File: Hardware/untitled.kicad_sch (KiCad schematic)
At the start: 15 parts, among them IC1 LM74502HDDFR, J3 CarLVPowerConnector, Q2 PSMN8R5-40MSDX

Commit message: BPS-Leader Schematic completed (mostly)
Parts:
- renumbered R18 to R51
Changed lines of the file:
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@@
 		(dnp no)
 		(fields_autoplaced yes)
-		(property "Reference" "R18"
+		(property "Reference" "R51"
 			(at 123.19 81.28 90)
 			(effects
@@
 			(project "BPS-Leader"
 				(path "/fb37da34-e420-4994-8cc1-079e8c0fa48e/a39d8cf5-dc9c-4f60-80f8-399517c69b53"
-					(reference "R18")
+					(reference "R51")
 					(unit 1)
 				)

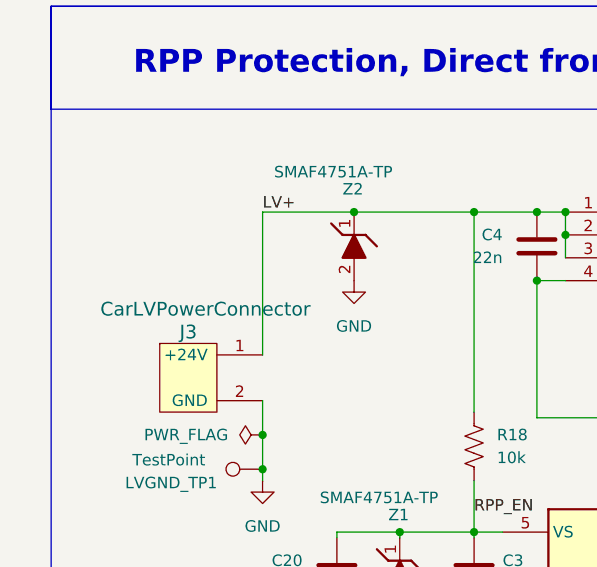
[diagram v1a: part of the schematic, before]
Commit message: added fuse, made kiCad Sharepoint a submodule, added a pulldown, added test-points
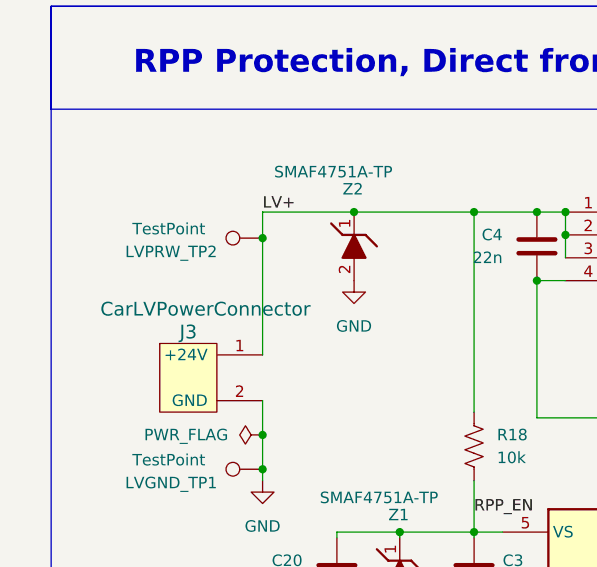
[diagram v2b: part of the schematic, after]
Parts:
- added LVPRW_TP2: TestPoint, UTSVT_Special:TestPoint_HEX_3mmID, symbol Connector:TestPoint
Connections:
- net LV+: now also LVPRW_TP2.1
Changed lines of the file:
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@@
+	)
+	(junction
+		(at 50.165 51.1574)
+		(diameter 0)
+		(color 0 0 0 0)
 	)
 	(junction
@@
 	(wire
 		(pts
+			(xy 50.165 51.1574) (xy 50.165 64.135)
+		)
+		(stroke
+			(width 0)
+			(type default)
+		)
+	)
+	(wire
+		(pts
 			(xy 73.66 48.26) (xy 80.645 48.26)
 		)
@@
 	(wire
 		(pts
-			(xy 50.165 48.26) (xy 50.165 64.135)
+			(xy 50.165 48.26) (xy 50.165 51.1574)
 		)
 		(stroke
@@
 					(unit 1)
 				)
+			)
+		)
+	)
+	(symbol
+		(lib_id "Connector:TestPoint")
+		(at 50.165 51.1574 90)
+		(unit 1)
+		(exclude_from_sim no)
+		(in_bom yes)
+		(on_board yes)
+		(dnp no)
+		(property "Reference" "LVPRW_TP2"
+			(at 40.005 52.6814 90)
+			(effects
+				(font
+					(size 1.27 1.27)
+				)
+			)
+		)
+		(property "Value" "TestPoint"
+			(at 39.751 50.1414 90)
+			(effects
+				(font
+					(size 1.27 1.27)
+				)
+			)
+		)
+		(property "Footprint" "UTSVT_Special:TestPoint_HEX_3mmID"
+			(at 50.165 46.0774 0)
+			(effects
+				(font
+					(size 1.27 1.27)
+				)
+				(hide yes)
+			)
+		)
+		(property "Datasheet" "~"
+			(at 50.165 46.0774 0)
+			(effects
+				(font
+					(size 1.27 1.27)
+				)
+				(hide yes)
+			)
+		)
+		(property "Description" "test point"
+			(at 50.165 51.1574 0)
+			(effects
+				(font
+					(size 1.27 1.27)
+				)
+				(hide yes)
+			)
+		)
+		(pin "1"
+		)
+		(instances
+			(project "BPS-Leader"
+				(path "/fb37da34-e420-4994-8cc1-079e8c0fa48e/a39d8cf5-dc9c-4f60-80f8-399517c69b53"
+					(reference "LVPRW_TP2")
+					(unit 1)
+				)

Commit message: Very, very intial layout designed. Many issues. Too bad!
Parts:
- 24V_TP1, LVGND_TP1, LVPRW_TP2: footprint UTSVT_Special:TestPoint_HEX_3mmID -> TestPoint:TestPoint_Pad_1.0x1.0mm
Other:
- note added: "3.3V injector"
- note removed: "3v3 injector"
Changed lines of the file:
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@@
 		)
 	)
-	(text "3v3 injector"
+	(text "3.3V injector"
 		(exclude_from_sim no)
 		(at 47.244 134.112 0)
@@
 			)
 		)
-		(property "Footprint" "UTSVT_Special:TestPoint_HEX_3mmID"
+		(property "Footprint" "TestPoint:TestPoint_Pad_1.0x1.0mm"
 			(at 50.165 71.755 0)
 			(effects
@@
 			)
 		)
-		(property "Footprint" "UTSVT_Special:TestPoint_HEX_3mmID"
+		(property "Footprint" "TestPoint:TestPoint_Pad_1.0x1.0mm"
 			(at 118.11 52.705 0)
 			(effects
@@
 			)
 		)
-		(property "Footprint" "UTSVT_Special:TestPoint_HEX_3mmID"
+		(property "Footprint" "TestPoint:TestPoint_Pad_1.0x1.0mm"
 			(at 50.165 46.0774 0)
 			(effects

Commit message: Backup
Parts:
- added D12: CDBC560-G, Schlotty:DIOM7959X262N, symbol Schott:CDBC560-G
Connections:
- net LV+: now also D12.2 (A); no longer C4.2, Q2.1 (S_1), Q2.2 (S_2), Q2.3 (S_3), R18.1
- new net: C4.2, D12.1 (K), Q2.1 (S_1), Q2.2 (S_2), Q2.3 (S_3), R18.1
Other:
- moved on the sheet: 24V_TP1, C20, C21, C3, C4, IC1, J3, LVGND_TP1, LVPRW_TP2, Q2, R18, R28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

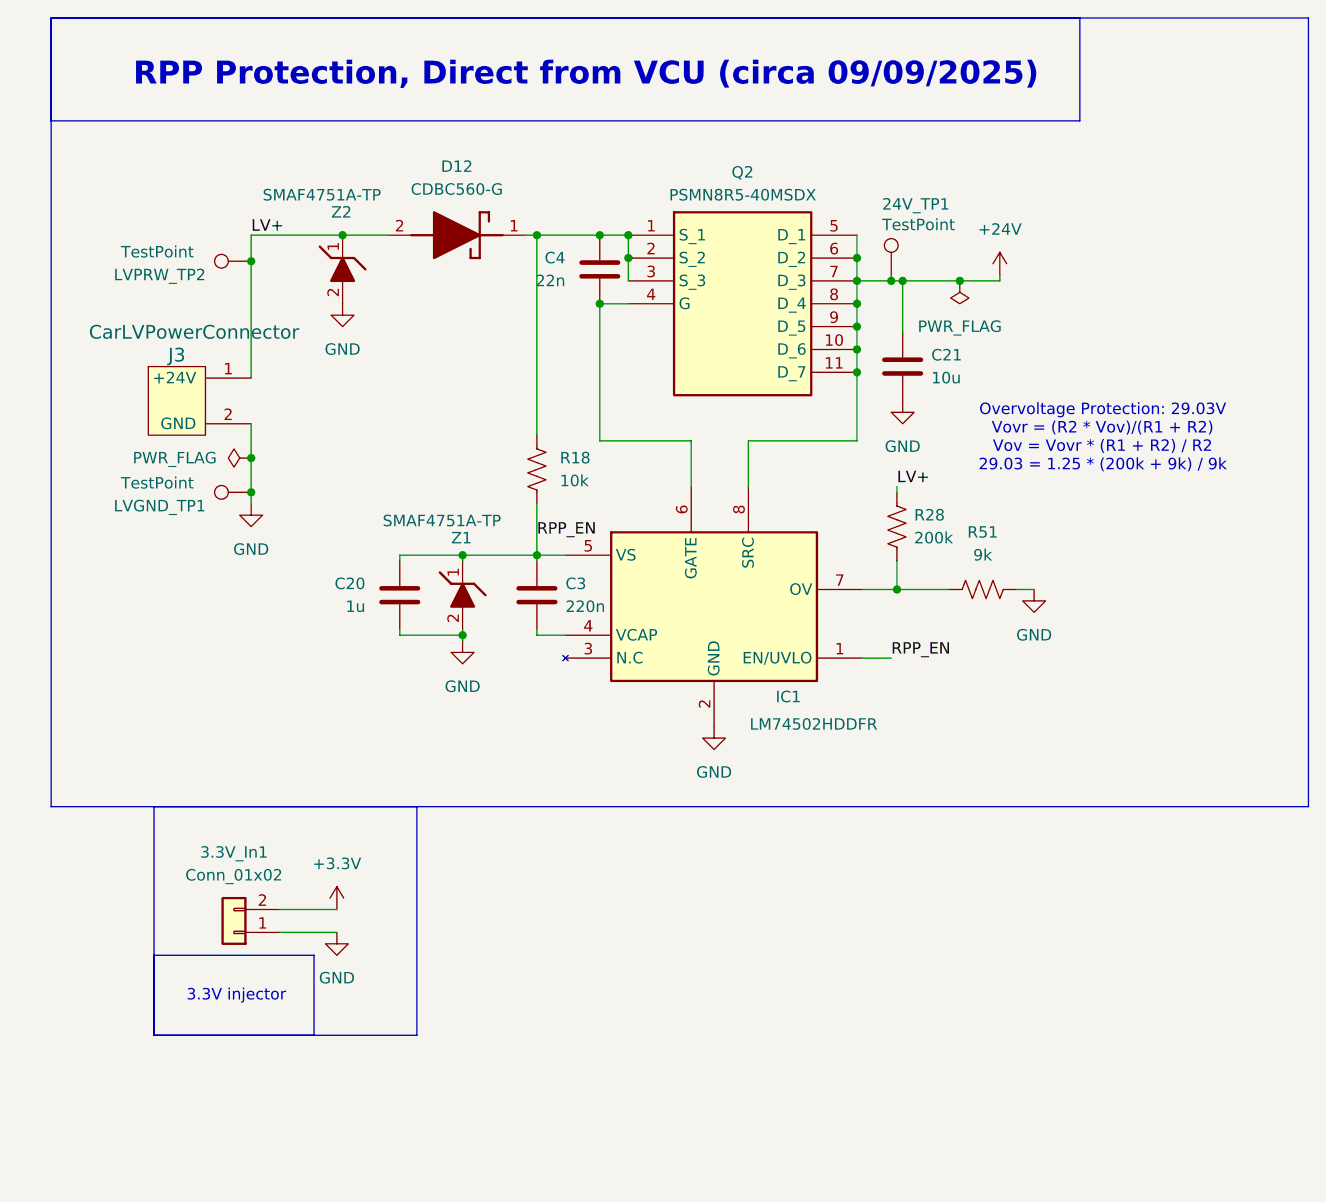
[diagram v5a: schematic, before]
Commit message: all 3d models added, minor fixes
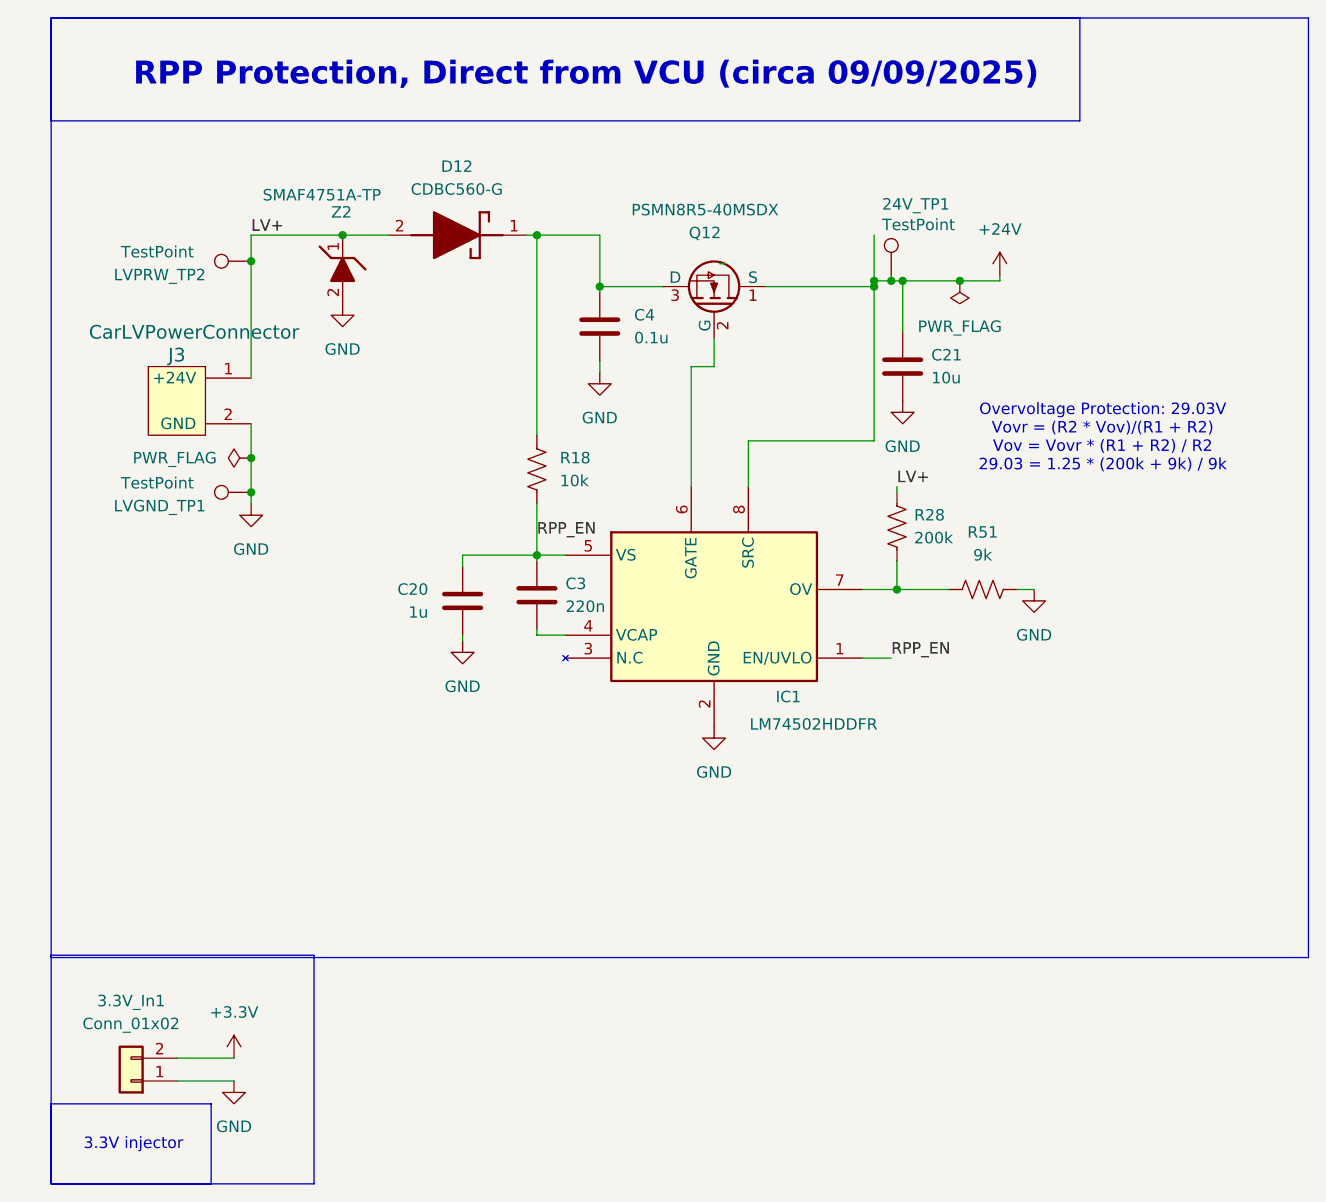
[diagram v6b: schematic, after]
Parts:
- removed Q2: PSMN8R5-40MSDX, UTSVT_Power:PSMN8R5-40MSDX, symbol UTSVT_Power:PSMN8R5-40MSDX
- removed Z1: SMAF4751A-TP, UTSVT_Passives:SODFL5026X125N, symbol UTSVT_Power:SMAF4749A-TP
- added Q12: PSMN8R5-40MSDX, UTSVT_Power:PSMN8R5-40MSDX, symbol utsvt_power:PSMN8R5-40MSDX
- C4: value 22n -> 0.1u; footprint Capacitor_SMD:C_0603_1608Metric -> Capacitor_SMD:C_0603_1608Metric_Pad1.08x0.95mm_HandSolder
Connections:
- net +24V: now also Q12.1 (S)
- net GND: now also C4.1
- net at IC1.6 (GATE): now also Q12.2 (G); no longer C4.1
- net at C4.2, D12.1 (K), R18.1: now also Q12.3 (D)
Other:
- moved on the sheet: 3.3V_In1, C20

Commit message: small fixes
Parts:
- C20: P/N (none) -> C0805C105K5PACTU
- C3: Manufactuerer (none) -> KYOCERA AVX; P/N (none) -> 06035C223K4T4A
- C4: Manufactuerer (none) -> TAIYO YUDEN; P/N (none) -> MLASH168SB7104KTNA01
- D12: Manufacturer_Part_Number CDBC560-G -> (none)
- IC1: Manufacturer_Part_Number LM74502HDDFR -> (none)
- Q12: Manufacturer_Part_Number PSMN8R5-40MSDX -> (none)
- Z2: Manufacturer_Part_Number SMAF4749A-TP -> (none)
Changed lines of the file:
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@@
-			)
-		)
-		(property "Manufacturer_Part_Number" "CDBC560-G"
-			(at 69.215 -744.12 0)
-			(effects
-				(font
-					(size 1.27 1.27)
-				)
-				(justify left top)
-				(hide yes)
 			)
 		)
@@
 			)
 		)
-		(property "Datasheet" "~"
+		(property "Datasheet" "https://datasheets.kyocera-avx.com/AutoMLCCKAM.pdf"
 			(at 80.645 89.535 0)
 			(effects
@@
 			)
 		)
-		(property "Manufactuerer" ""
+		(property "Manufactuerer" "KYOCERA AVX "
+			(at 80.645 89.535 0)
+			(effects
+				(font
+					(size 1.27 1.27)
+				)
+				(hide yes)
+			)
+		)
+		(property "P/N" "06035C223K4T4A "
 			(at 80.645 89.535 0)
 			(effects
@@
 			)
 		)
-		(property "Datasheet" "~"
+		(property "Datasheet" "https://ds.yuden.co.jp/TYCOMPAS/or/download?pn=MLAST063SCG681JFNA01&fileType=CA"
 			(at 87.63 59.69 0)
 			(effects
@@
 			)
 		)
-		(property "Manufactuerer" ""
+		(property "Manufactuerer" "TAIYO YUDEN "
+			(at 87.63 59.69 0)
+			(effects
+				(font
+					(size 1.27 1.27)
+				)
+				(hide yes)
+			)
+		)
+		(property "P/N" "MLASH168SB7104KTNA01 "
 			(at 87.63 59.69 0)
 			(effects
@@
 		(property "Manufacturer_Name" "Texas Instruments"
 			(at 113.03 780.01 0)
-			(effects
-				(font
-					(size 1.27 1.27)
-				)
-				(justify left top)
-				(hide yes)
-			)
-		)
-		(property "Manufacturer_Part_Number" "LM74502HDDFR"
-			(at 113.03 880.01 0)
 			(effects
 				(font
@@
 			)
 		)
-		(property "Manufacturer_Part_Number" "SMAF4749A-TP"
-			(at -734.595 57.15 0)
-			(effects
-				(font
-					(size 1.27 1.27)
-				)
-				(justify left top)
-				(hide yes)
-			)
-		)
 		(property "Manufactuerer" ""
 			(at 59.055 46.99 90)
@@
 			)
 		)
+		(property "P/N" "C0805C105K5PACTU"
+			(at 72.39 90.17 0)
+			(effects
+				(font
+					(size 1.27 1.27)
+				)
+				(hide yes)
+			)
+		)
 		(pin "2"
 		)
@@
 			(effects
 				(font
-					(size 1.27 1.27)
-				)
-				(justify left top)
-				(hide yes)
-			)
-		)
-		(property "Manufacturer_Part_Number" "PSMN8R5-40MSDX"
-			(at 78.74 849.53 0)
-			(effects
-				(font
